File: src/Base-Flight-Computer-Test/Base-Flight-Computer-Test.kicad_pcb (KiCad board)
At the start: 4 copper layers, 41 x 20.3 mm, 58 parts, among them J1 Jumper_NO, P1 1984659, P2 USB, P3 0530470610, P4 1984659, P5 B2B-PH-K-SLFSN_JST, Q1 QS5U17TR, Q2 2N7002W-7-F, Q3 2N7002W-7-F, Q4 QS5U17TR, Q5 2N7002W-7-F, Q6 2N7002W-7-F, U1 STM32G4A1KEU6, U2 BMP390, U3 LMS8117AMP-3.3_NOPB, U4 SST25VF040B-50-4I-S2AE-T, Y1 ECS-240-18-33-JGN-TR

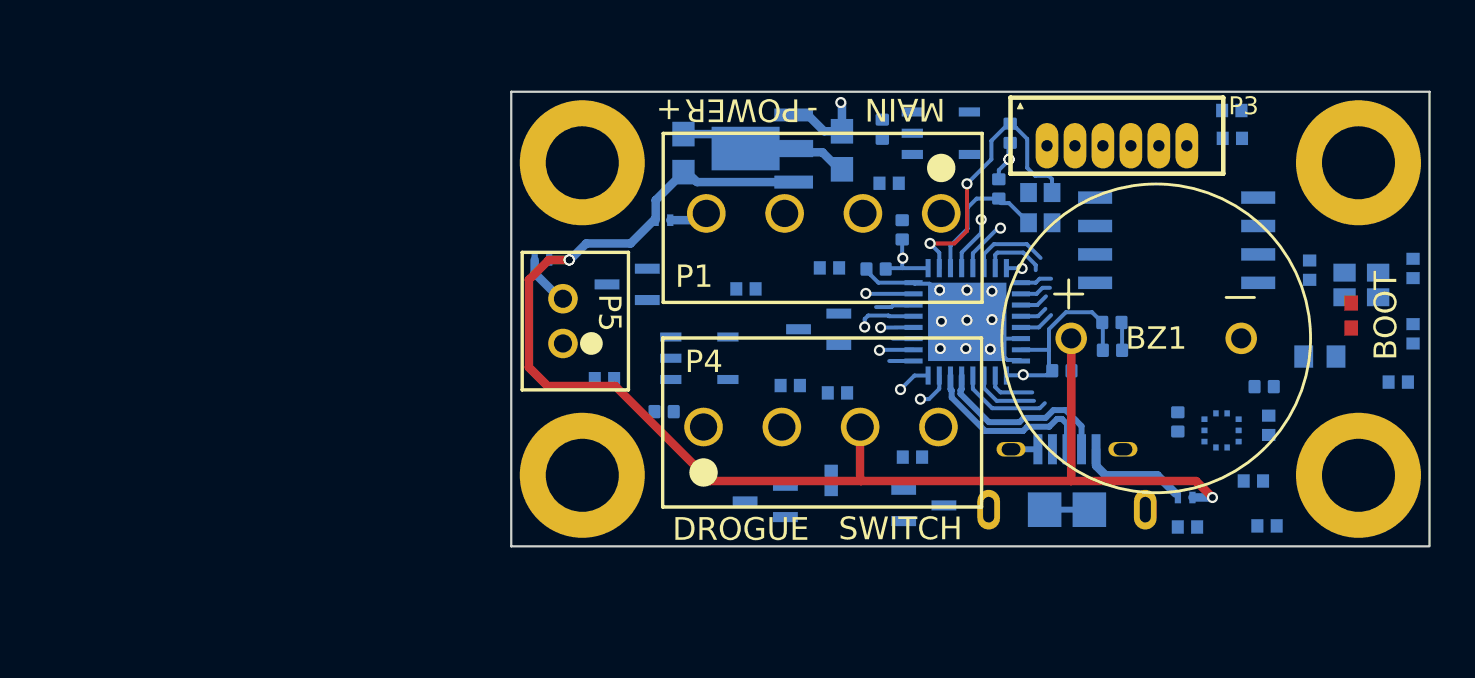
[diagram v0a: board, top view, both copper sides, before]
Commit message: placed components on test board
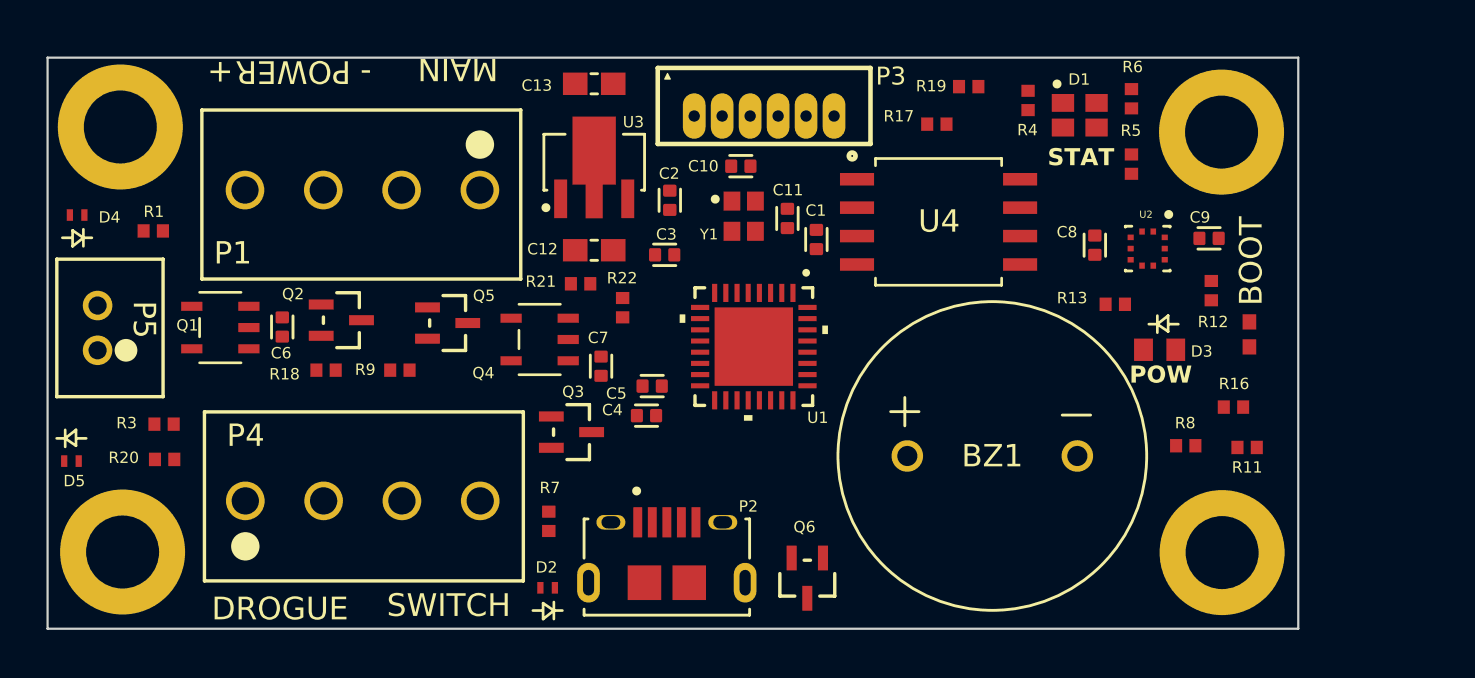
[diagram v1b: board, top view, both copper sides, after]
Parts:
- C1, C10, C11, C12, C13, C2, C3, C4, C5, C6, C7, C8, C9, D1, D2, D3, D4, D5, P2, Q1, Q2, Q3, Q4, Q5, Q6, R1, R11, R12, R13, R16, R17, R18, R19, R20, R21, R22, R3, R4, R5, R6, R7, R8, R9, U1, U2, U3, U4, Y1: moved to F.Cu
- moved R3 34.2 mm to (111.5, 96.1), turned to 0 degrees
- moved R20 33.4 mm to (111.5, 97.7), turned to 0 degrees
- moved Q1 33.4 mm to (114.0, 91.8), turned to 180 degrees
- moved R1 30.3 mm to (111.0, 87.5), turned to 0 degrees
- moved D2 28.8 mm to (128.6, 103.5)
- moved C6 28.2 mm to (116.8, 91.8)
- moved D4 26.2 mm to (107.6, 86.8), turned to 180 degrees
- moved R18 23.1 mm to (118.7, 93.7), turned to 180 degrees
- moved D5 22.9 mm to (107.3, 97.8), turned to 0 degrees
- moved C4 21.0 mm to (133.0, 95.8), turned to 180 degrees
- moved H4 20.8 mm to (109.6, 101.9)
- moved P5 20.8 mm to (108.5, 92.8)
- moved P4 20.7 mm to (115.1, 99.6)
- moved C5 20.7 mm to (133.3, 94.4), turned to 180 degrees
- moved H2 20.7 mm to (109.5, 82.9)
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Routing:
- net VIN: track 61.0 -> 0.00 mm, vias 3 -> 0
- net Earth: track 18.0 -> 0.00 mm, vias 11 -> 0
- net 3.3V: track 15.5 -> 0.00 mm, vias 3 -> 0
- net OSC_IN: track 12.8 -> 0.00 mm, vias 2 -> 0
- net USB_D-: track 8.48 -> 0.00 mm
- net USB_D+: track 8.22 -> 0.00 mm
- net OSC_OUT: track 6.03 -> 0.00 mm
- net 5V: track 4.80 -> 0.00 mm
- net USB_DETECT: track 4.27 -> 0.00 mm
- net ~{SWITCH}: track 3.60 -> 0.00 mm
- net BP_SCL: track 3.03 -> 0.00 mm
- net BEEP: track 2.91 -> 0.00 mm
- net STATUS_G: track 2.75 -> 0.00 mm, vias 1 -> 0
- net NRST: track 2.53 -> 0.00 mm, vias 1 -> 0
- net VBAT_SENSE: track 2.37 -> 0.00 mm, vias 1 -> 0
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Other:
- board size 41 x 20.3 mm -> 55.9 x 25.5 mm

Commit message: updated DRC ruleset
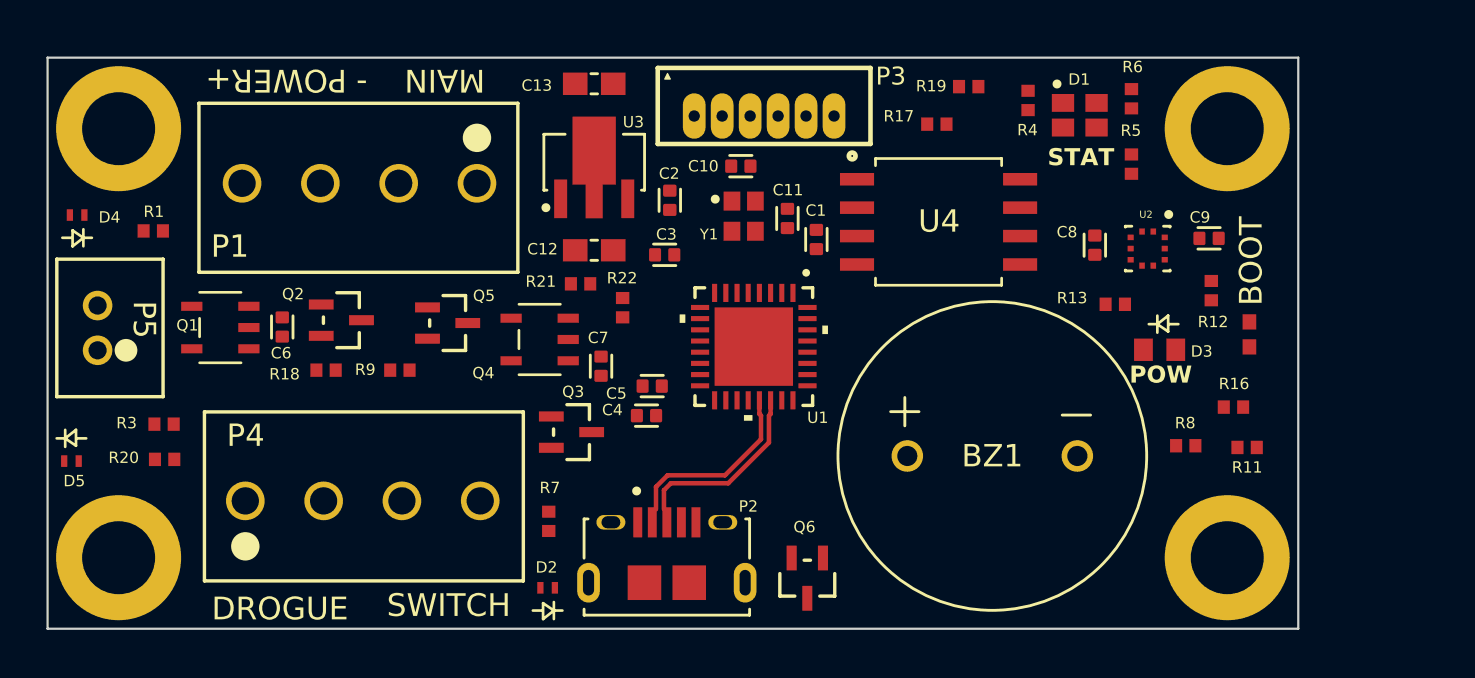
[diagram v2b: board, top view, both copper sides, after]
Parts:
- moved P1 0.33 mm to (125.5, 85.4)
- moved H3 0.32 mm to (159.0, 102.1)
- moved H4 0.31 mm to (109.4, 102.1)
- moved H1 0.30 mm to (159.0, 82.9)
- moved H2 0.11 mm to (109.4, 82.9)
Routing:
- net USB_D-: track 0.00 -> 8.35 mm
- net USB_D+: track 0.00 -> 8.35 mm
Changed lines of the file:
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@@
   )
   (footprint "Base-Flight-Computer:MountingHole_4-40" (layer "F.Cu")
-    (at 109.6264 101.854)
+    (at 109.4486 102.108)
     (descr "Mounting Hole 3mm")
     (tags "mounting hole 3mm")
@@
   )
   (footprint "Base-Flight-Computer:MountingHole_4-40" (layer "F.Cu")
-    (at 158.7754 101.8794)
+    (at 159.004 102.108)
     (descr "Mounting Hole 3mm")
     (tags "mounting hole 3mm")
@@
   )
   (footprint "Base-Flight-Computer:1546551-4" (layer "F.Cu")
-    (at 125.597801 85.6742 180)
+    (at 125.4674 85.3726 180)
     (tags "1546551-4 ")
     (property "Sheetfile" "Base-Flight-Computer.kicad_sch")
@@
   )
   (footprint "Base-Flight-Computer:MountingHole_4-40" (layer "F.Cu")
-    (at 158.75 83.0834)
+    (at 159.004 82.931)
     (descr "Mounting Hole 3mm")
     (tags "mounting hole 3mm")
@@
   )
   (footprint "Base-Flight-Computer:MountingHole_4-40" (layer "F.Cu")
-    (at 109.5248 82.8548)
+    (at 109.4486 82.931)
     (descr "Mounting Hole 3mm")
     (tags "mounting hole 3mm")
@@
     (effects (font (size 0.762 0.762) (thickness 0.127) bold))
   )
-  (gr_text "MAIN" (at 124.615801 80.2608 180) (layer "F.SilkS")
+  (gr_text "MAIN" (at 124.0282 80.772 180) (layer "F.SilkS")
     (effects (font (size 1.016 1.016) (thickness 0.2032)))
   )
@@
     (effects (font (size 1.016 1.016) (thickness 0.2032)))
   )
-  (gr_text "+" (at 114.024001 80.3878 270) (layer "F.SilkS")
+  (gr_text "+" (at 113.9444 80.7212 270) (layer "F.SilkS")
     (effects (font (size 1.016 1.016) (thickness 0.2032)))
   )
-  (gr_text "-" (at 120.501001 80.2862) (layer "F.SilkS")
+  (gr_text "-" (at 120.3198 80.7466) (layer "F.SilkS")
     (effects (font (size 1.016 1.016) (thickness 0.2032)))
   )
-  (gr_text "POWER" (at 117.249801 80.3878 180) (layer "F.SilkS")
+  (gr_text "POWER" (at 117.0686 80.772 180) (layer "F.SilkS")
     (effects (font (size 1.016 1.016) (thickness 0.2032)))
   )
@@
     (effects (font (size 1.016 1.016) (thickness 0.2032)))
   )
+  (segment (start 138.164189 95.754064) (end 138.164189 96.813763) (width 0.2032) (layer "F.Cu") (net 17))
+  (segment (start 133.987552 98.425) (end 133.469341 98.943211) (width 0.2032) (layer "F.Cu") (net 17))
+  (segment (start 138.164189 96.813763) (end 136.552952 98.425) (width 0.2032) (layer "F.Cu") (net 17))
+  (segment (start 138.091926 95.0722) (end 138.091926 95.681801) (width 0.2032) (layer "F.Cu") (net 17))
+  (segment (start 138.091926 95.681801) (end 138.164189 95.754064) (width 0.2032) (layer "F.Cu") (net 17))
+  (segment (start 133.469341 98.943211) (end 133.469341 99.947674) (width 0.2032) (layer "F.Cu") (net 17))
+  (segment (start 136.552952 98.425) (end 133.987552 98.425) (width 0.2032) (layer "F.Cu") (net 17))
+  (segment (start 138.592052 95.0722) (end 138.592052 95.681801) (width 0.2032) (layer "F.Cu") (net 18))
+  (segment (start 133.824941 99.090507) (end 133.824941 99.947674) (width 0.2032) (layer "F.Cu") (net 18))
+  (segment (start 138.519789 95.754064) (end 138.519789 96.961059) (width 0.2032) (layer "F.Cu") (net 18))
+  (segment (start 138.592052 95.681801) (end 138.519789 95.754064) (width 0.2032) (layer "F.Cu") (net 18))
+  (segment (start 136.700248 98.7806) (end 134.134848 98.7806) (width 0.2032) (layer "F.Cu") (net 18))
+  (segment (start 138.519789 96.961059) (end 136.700248 98.7806) (width 0.2032) (layer "F.Cu") (net 18))
+  (segment (start 134.134848 98.7806) (end 133.824941 99.090507) (width 0.2032) (layer "F.Cu") (net 18))
 )

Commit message: completed initial test layout
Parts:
- moved R11 19.7 mm to (140.3, 99.1)
- moved R20 17.4 mm to (128.8, 100.0), turned to 90 degrees
- moved R7 17.2 mm to (111.7, 98.1), turned to 0 degrees
- moved R8 17.0 mm to (140.4, 100.4)
- moved C7 14.3 mm to (116.8, 92.4)
- moved Q4 14.3 mm to (114.0, 92.0)
- moved Q3 11.4 mm to (119.4, 91.6), turned to 0 degrees
- moved C2 11.3 mm to (133.1, 97.4), turned to 180 degrees
- moved R9 10.8 mm to (111.6, 96.6)
- moved Q1 9.50 mm to (123.5, 91.6)
- moved C6 9.37 mm to (126.1, 91.8)
- moved Q2 9.12 mm to (128.5, 92.2), turned to 0 degrees
- moved R3 8.36 mm to (119.7, 94.5)
- moved C3 8.08 mm to (135.0, 96.6), turned to 180 degrees
- moved Q5 7.38 mm to (129.7, 96.4)
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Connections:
- U1 pad 27: DROGUE -> BEEP
- U1 pad 7: BEEP -> STATUS_B
- U1 pad 9: STATUS_B -> DROGUE
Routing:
- net VIN: track 0.00 -> 114.7 mm, vias 0 -> 3
- net Earth: track 0.00 -> 92.1 mm, vias 0 -> 19
- net 3.3V: track 0.00 -> 69.7 mm, vias 0 -> 12
- net VIN_SW: track 0.00 -> 53.9 mm
- net ~{DROGUE_CONT}: track 0.00 -> 52.3 mm, vias 0 -> 2
- net ~{MAIN_CONT}: track 0.00 -> 51.9 mm, vias 0 -> 2
- net ~{FLASH_SS}: track 0.00 -> 29.0 mm, vias 0 -> 2
- net BP_SCL: track 0.00 -> 28.7 mm, vias 0 -> 2
- net BP_SDA: track 0.00 -> 27.7 mm, vias 0 -> 2
- net DROGUE: track 0.00 -> 26.4 mm, vias 0 -> 2
- net FLASH_SCK: track 0.00 -> 25.0 mm, vias 0 -> 2
- net FLASH_MOSI: track 0.00 -> 23.1 mm, vias 0 -> 2
- net STATUS_B: track 0.00 -> 22.7 mm, vias 0 -> 2
- net FLASH_MISO: track 0.00 -> 22.7 mm, vias 0 -> 2
- net BOOT: track 0.00 -> 21.6 mm, vias 0 -> 4
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- added copper zone on In2.Cu, net 3.3V
- added copper zone on B.Cu, net Earth
- added copper zone on In1.Cu, net Earth

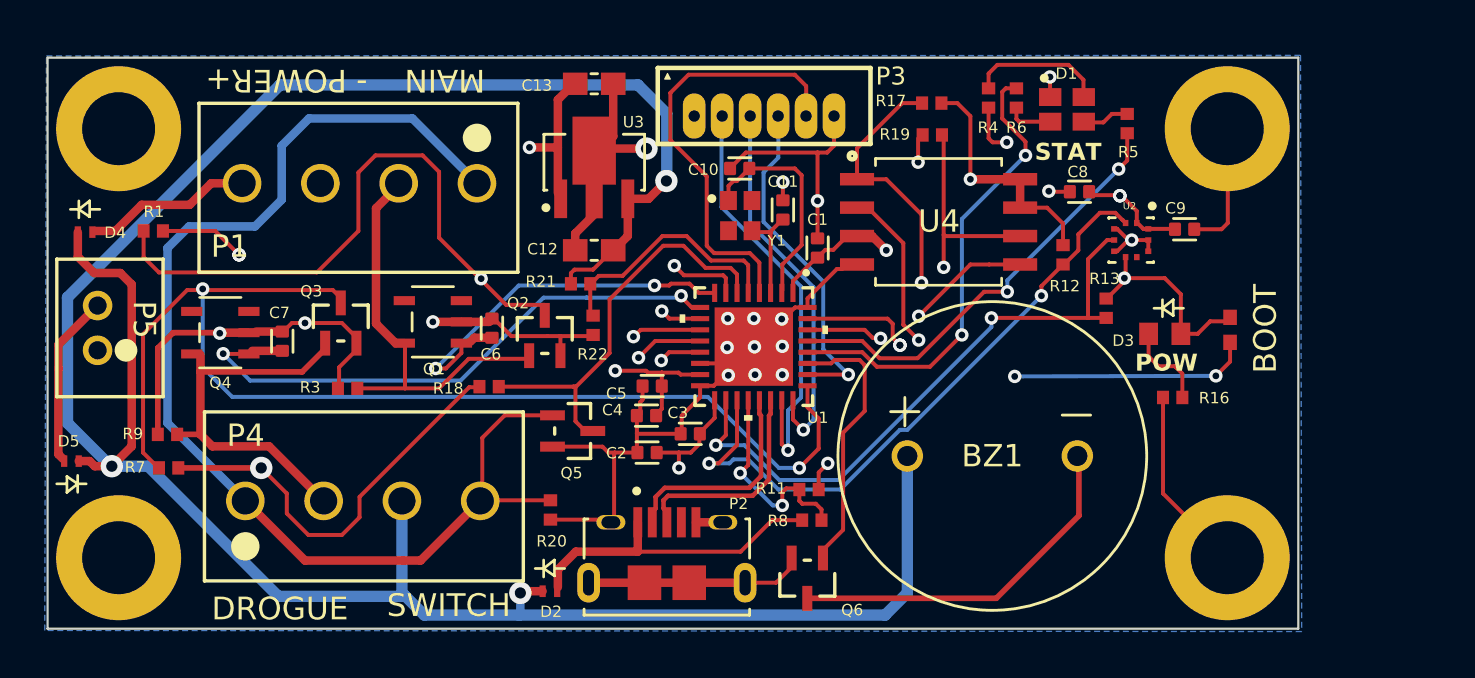
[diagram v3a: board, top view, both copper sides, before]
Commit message: resolved DRC issues with Test layout
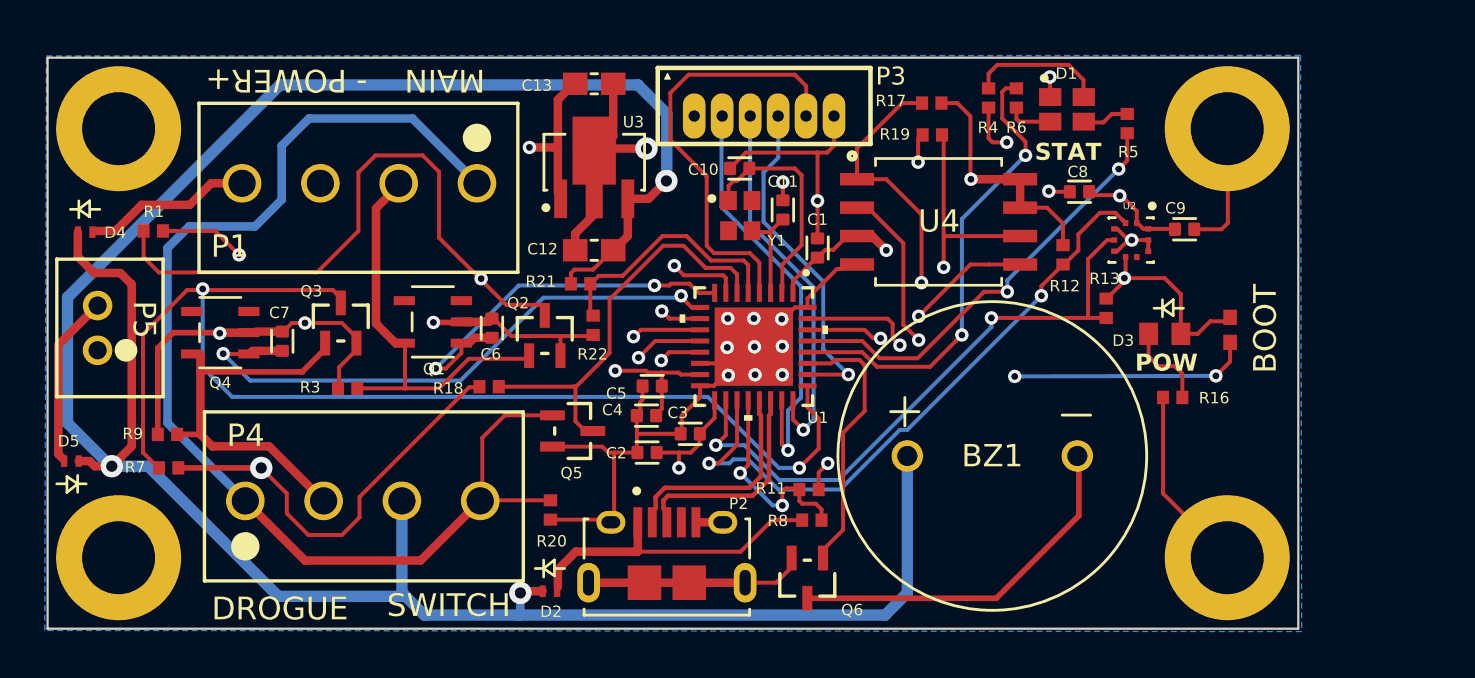
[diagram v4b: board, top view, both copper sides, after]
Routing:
- net Earth: track 92.1 -> 91.5 mm
- net 3.3V: track 69.7 -> 69.4 mm, vias 12 -> 10
- net BOOT: track 21.6 -> 21.5 mm, vias 4 -> 3
